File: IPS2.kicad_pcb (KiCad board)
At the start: 2 copper layers, 26 x 108 mm, 62 parts, among them J1 USB_C_Receptacle, J2 CONN_01X02_MALE, J3 CONN_01X02_MALE, J4 USB_C_Receptacle, J5 GS2, J6 GS2, P1 CONN_02X05, Q1 Q_NPN_BEC, Q2 Q_NPN_BEC, T1 TESTPIN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

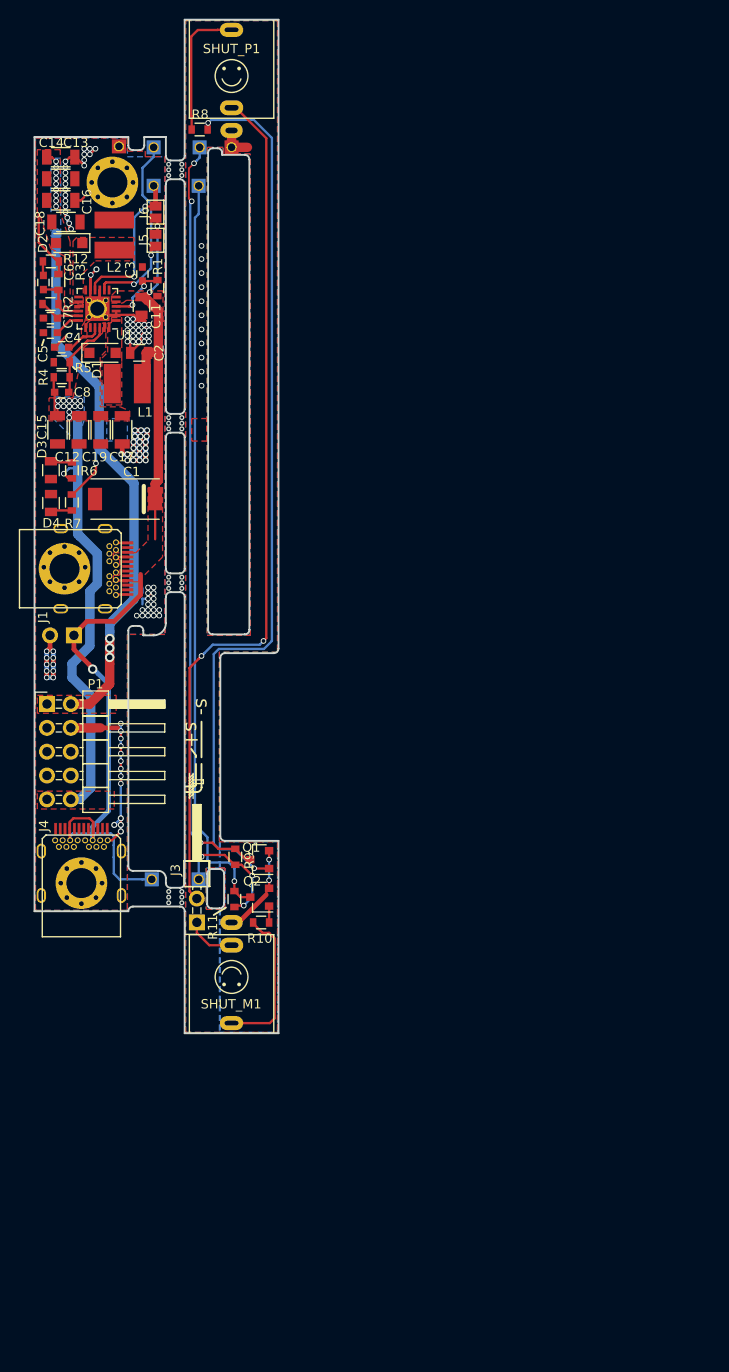
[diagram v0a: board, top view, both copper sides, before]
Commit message: Update PCB with linked panel with break-tab. Changed USB socket.
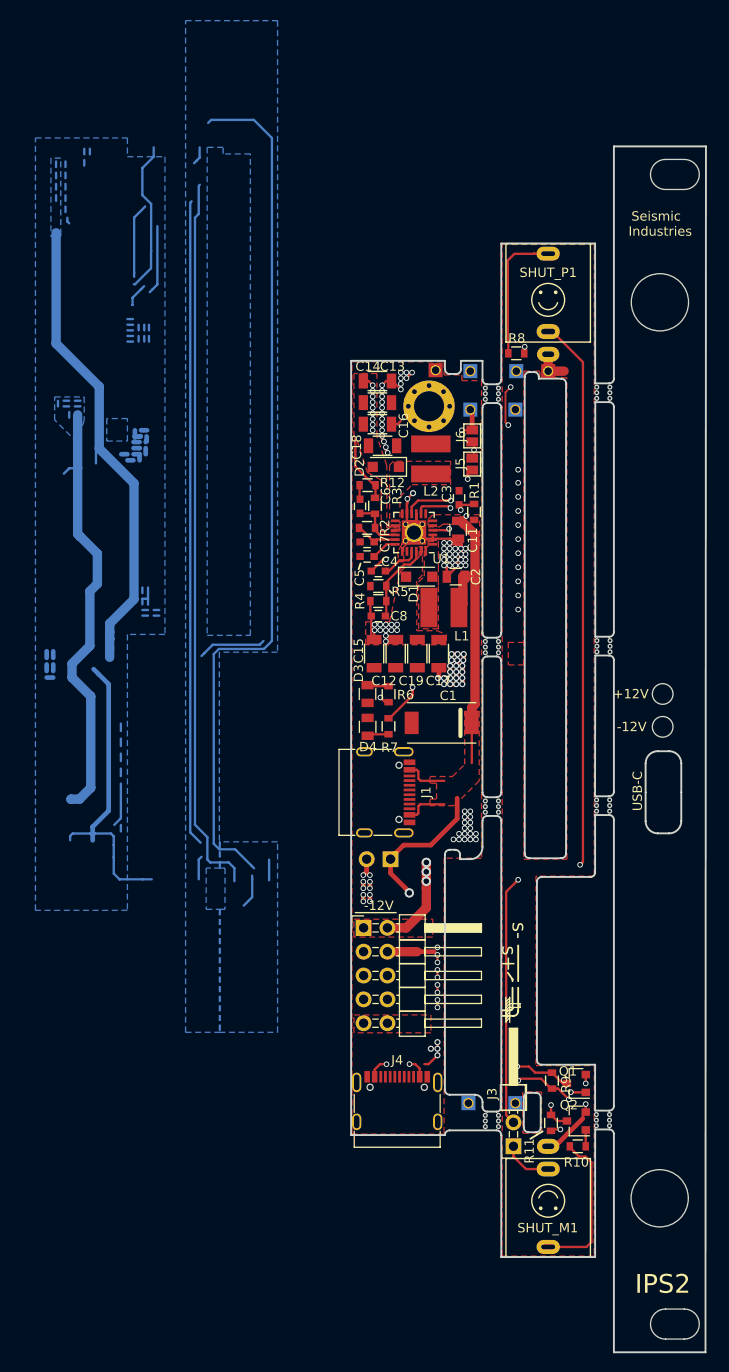
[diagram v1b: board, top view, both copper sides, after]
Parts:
- removed T10, T11: TESTPIN, raffilibkicad:VIA_M3_mounting_hole
- added ?: , , F.Cu at (66.9, 71.8)
- added ?: , , F.Cu at (66.6, 125.6)
- added ?: , , F.Cu at (66.6, 30.1)
- added ?: , , F.Cu at (66.9, 75.3)
- added REF**: break_tab, raffilibkicad:break_tab, F.Cu at (60.6, 39.8)
- added REF**: break_tab, raffilibkicad:break_tab, F.Cu at (60.6, 117.3)
- added REF**: break_tab, raffilibkicad:break_tab, F.Cu at (60.6, 83.7)
- added REF**: break_tab, raffilibkicad:break_tab, F.Cu at (60.6, 66.8)
- J1, J4: footprint raffilibkicad:USB_TYPE_C_WUERTH_632723300011 -> Connector_USB:USB_C_Receptacle_G-Switch_GT-USB-7010ASV
- moved J1 43.9 mm to (36.2, 82.3)
- moved C1 41.3 mm to (43.4, 74.9)
- moved C11 41.3 mm to (45.1, 54.4)
- moved C12 41.3 mm to (38.5, 67.5)
- moved C13 41.3 mm to (36.5, 40.8)
- moved C14 41.3 mm to (36.5, 38.5)
- moved C16 41.3 mm to (36.5, 43.1)
- moved C17 41.3 mm to (43.1, 67.5)
- moved C18 41.3 mm to (37.1, 45.4)
- moved C19 41.3 mm to (40.8, 67.5)
- moved C2 41.3 mm to (44.9, 59.4)
- moved C3 41.3 mm to (45.2, 51.0)
- moved C4 41.3 mm to (36.6, 58.8)
- moved C8 41.3 mm to (36.6, 63.5)
- moved D1 41.3 mm to (41.0, 59.4)
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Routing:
- net V_INPUT: track 114.4 -> 119.0 mm, vias 6 -> 8
- net Earth: track 125.1 -> 122.5 mm
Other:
- board size 26 x 108 mm -> 37.8 x 128.5 mm
- net class Default removed
- board text added: "+12V"
- board text added: "-12V"
- board text added: "IPS2"
- board text added: "Seismic Industries"
- board text added: "USB-C"
- board text removed: "1.6 * 4.2 mm cutout"

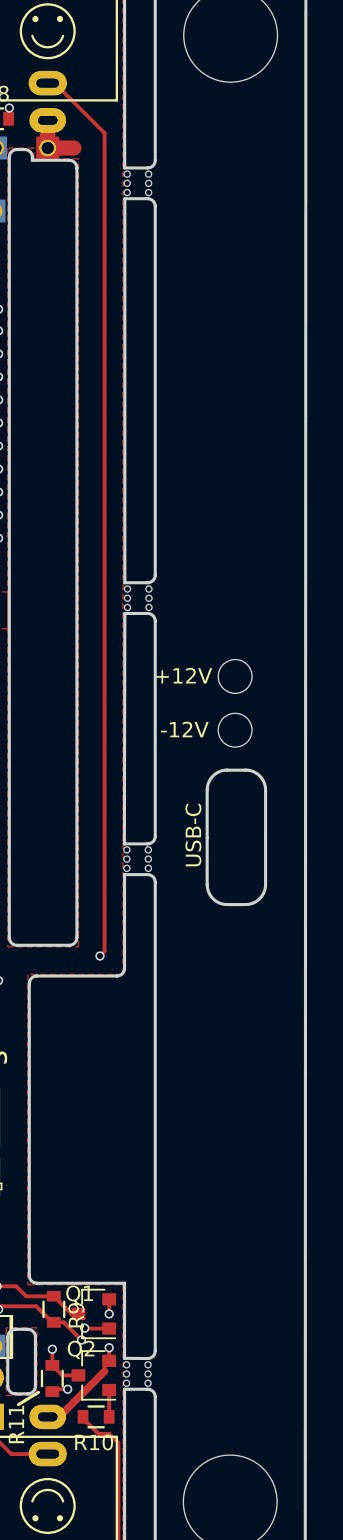
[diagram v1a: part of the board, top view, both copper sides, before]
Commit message: Add labels to shut jacks. Update readme.
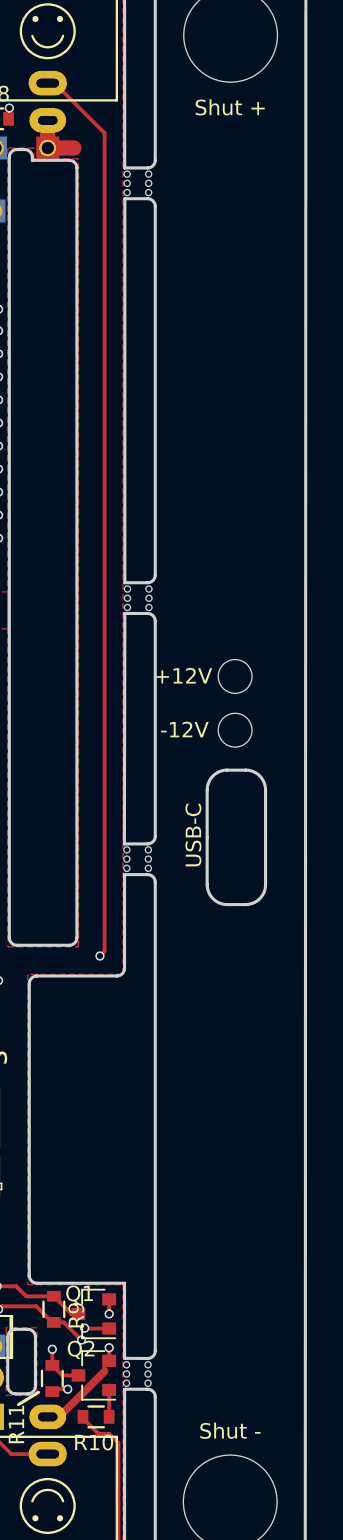
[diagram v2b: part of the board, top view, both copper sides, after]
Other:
- board text added: "Shut +"
- board text added: "Shut -"
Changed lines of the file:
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@@
 		)
 		(property "Value" "USB_C_Receptacle"
-			(at 0 5 270)
+			(at 0 5 -90)
 			(layer "F.Fab")
 			(hide yes)
@@
 		)
 	)
+	(gr_text "Shut -"
+		(at 66.62 121 0)
+		(layer "F.SilkS")
+		(effects
+			(font
+				(size 1 1)
+				(thickness 0.15)
+			)
+		)
+	)
 	(gr_text "+12V"
 		(at 63.54 71.85 0)
 		(layer "F.SilkS")
 		(effects
+			(font
+				(size 1 1)
+				(thickness 0.15)
+			)
+		)
+	)
+	(gr_text "Shut +"
+		(at 66.645 34.85 0)
+		(layer "F.SilkS")
+		(effects
